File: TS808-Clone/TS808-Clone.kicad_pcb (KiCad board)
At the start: 2 copper layers, 78.7 x 147.3 mm, 44 parts, among them J1 AudioJack2, J2 Barrel_Jack, J3 AudioJack2, Q1 2N4401-AP, Q2 2N4401-AP, U1 RC4558

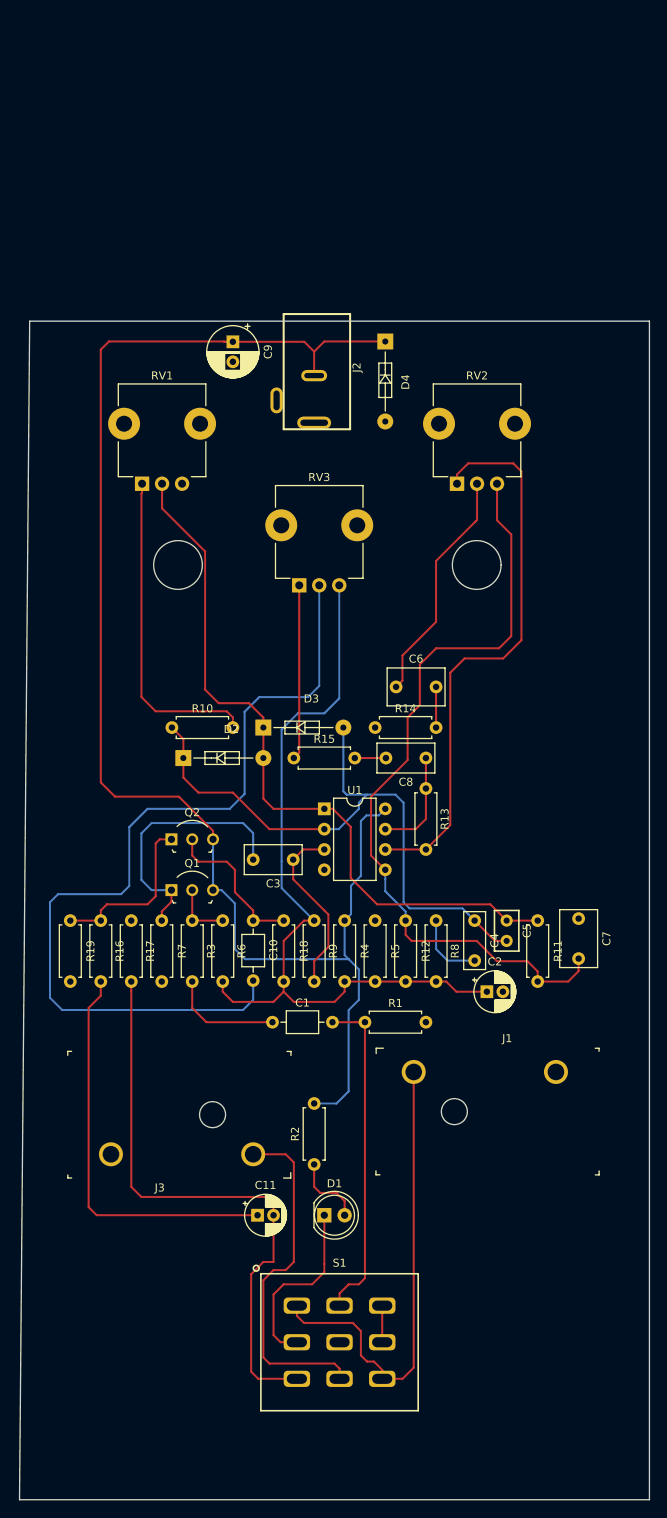
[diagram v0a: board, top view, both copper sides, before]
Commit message: Generally rearranged tracks and a couple componenets. Removed holes.
Is now cleaner. Holes+standoffs were not needed because the pots are panel mount.
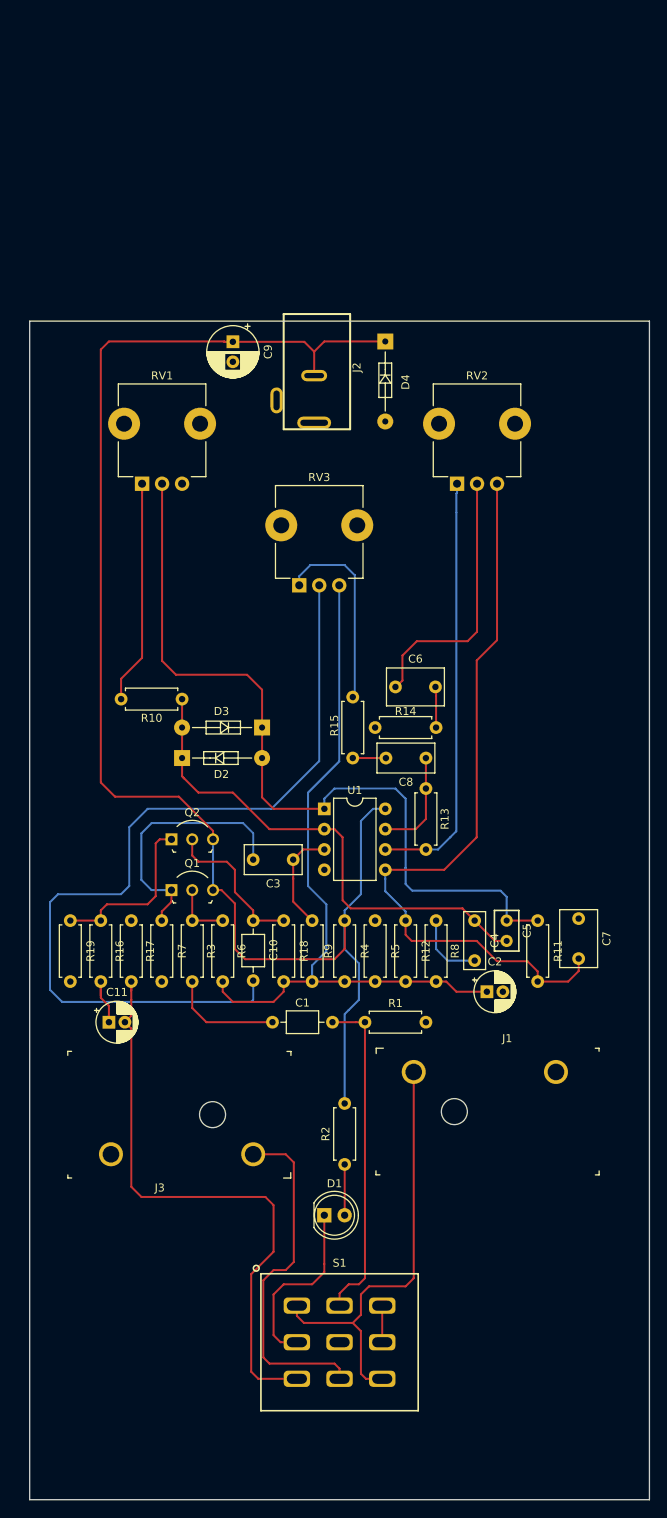
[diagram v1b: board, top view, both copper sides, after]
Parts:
- moved C11 30.5 mm to (100.1, 109.2)
- moved R15 10.6 mm to (130.6, 68.6), turned to 270 degrees
- moved R9 7.62 mm to (125.5, 104.1), turned to 90 degrees
- moved R2 3.81 mm to (129.5, 127.0)
- moved R10 3.78 mm to (109.2, 68.8), turned to 180 degrees
- moved D2 0.16 mm to (109.2, 76.2)
- moved D3 0.16 mm to (119.2, 72.4), turned to 180 degrees
- moved C6 0.08 mm to (135.9, 67.3)
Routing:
- net Net-(C11-Pad1): track 50.4 -> 7.28 mm
- net Net-(R13-Pad2): track 70.3 -> 53.3 mm
- net Net-(C4-Pad1): track 78.1 -> 63.5 mm
- net Net-(R10-Pad2): track 40.5 -> 29.2 mm
- net Net-(C5-Pad1): track 91.2 -> 101.5 mm
- net Net-(C3-Pad1): track 22.2 -> 13.1 mm
- net Net-(C2-Pad1): track 97.9 -> 90.0 mm
- net Net-(C6-Pad1): track 29.6 -> 33.3 mm
- net Net-(J1-PadT): track 59.1 -> 55.5 mm
- net Net-(D1-Pad2): track 9.12 -> 5.59 mm
- net Net-(C7-Pad2): track 97.7 -> 94.4 mm
- net Net-(R15-Pad1): track 21.9 -> 24.4 mm
- net Net-(C10-Pad1): track 108.7 -> 106.7 mm
- net Net-(C11-Pad2): track 73.2 -> 74.2 mm
- net VS: track 186.5 -> 187.1 mm
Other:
- board size 78.7 x 147.3 mm -> 77.5 x 147.3 mm
- rule trace_min: 0.1524 -> 0.2032

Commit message: Finished traces. Added fill with ground layer.
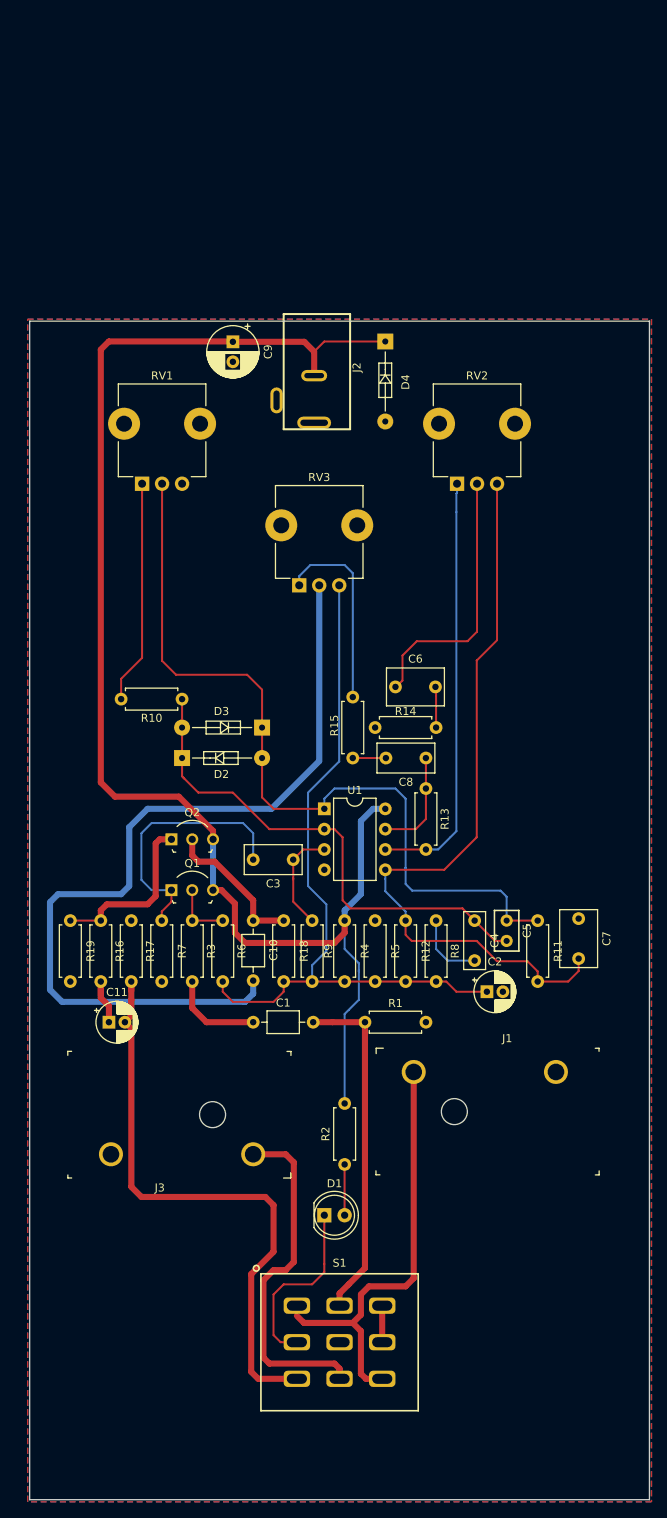
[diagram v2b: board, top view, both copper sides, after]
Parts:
- moved C1 2.41 mm to (118.1, 109.2)
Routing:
- net VS: track 187.1 -> 184.0 mm
- net Net-(C1-Pad1): track 14.1 -> 11.7 mm
- net Net-(C1-Pad2): track 41.6 -> 43.2 mm
- net Net-(C10-Pad2): track 19.2 -> 18.3 mm
- added copper zone on B.Cu, net GNDREF
- added copper zone on F.Cu, net GNDREF
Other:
- net class Default: clearance 0.2 -> 0.2032; trace_width 0.25 -> 0.762
- rule trace_clearance: 0.2 -> 0.2032

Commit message: trying a redesign of the layout
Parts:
- RV1: value 500k -> 500k LOG
- RV2: value 20k -> 20k LIN
- RV3: value 100k -> 100k LOG
- moved R5 112.5 mm to (138.6, -8.19), turned to 0 degrees
- moved R4 108.3 mm to (127.9, -4.14), turned to 0 degrees
- moved C2 108.2 mm to (161.0, -1.89)
- moved R17 67.1 mm to (114.9, 162.6), turned to 90 degrees
- moved R18 61.6 mm to (130.8, 43.2), turned to 270 degrees
- moved C10 61.4 mm to (127.0, 43.3), turned to 270 degrees
- moved R11 59.4 mm to (114.3, 59.7)
- moved C5 58.4 mm to (106.7, 58.4)
- moved C4 56.6 mm to (102.9, 59.6), turned to 90 degrees
- moved R14 49.8 mm to (163.8, 33.0), turned to 270 degrees
- moved Q2 47.6 mm to (121.2, 132.1)
- moved R8 44.1 mm to (111.8, 63.5)
- moved R16 43.6 mm to (114.9, 137.2)
- moved C11 41.9 mm to (114.3, 148.6), turned to 270 degrees
- moved C7 41.3 mm to (127.0, 69.8), turned to 0 degrees
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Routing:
- net VS: track 184.0 -> 0.00 mm
- net Net-(C10-Pad1): track 106.3 -> 0.00 mm
- net Net-(C5-Pad1): track 101.5 -> 0.00 mm
- net Net-(C7-Pad2): track 94.4 -> 0.00 mm
- net Net-(C2-Pad1): track 90.0 -> 0.00 mm
- net Net-(C11-Pad2): track 74.2 -> 0.00 mm
- net Net-(C4-Pad1): track 63.5 -> 0.00 mm
- net Net-(J1-PadT): track 55.5 -> 0.00 mm
- net Net-(R13-Pad2): track 53.3 -> 0.00 mm
- net Net-(J3-PadT): track 43.7 -> 0.00 mm
- net Net-(C1-Pad2): track 43.2 -> 0.00 mm
- net Net-(C6-Pad1): track 33.3 -> 0.00 mm
- net Net-(C3-Pad2): track 32.8 -> 0.00 mm
- net Net-(R10-Pad2): track 29.2 -> 0.00 mm
- net Net-(R15-Pad1): track 24.3 -> 0.00 mm
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
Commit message: moved jacks to final positions
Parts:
- D1: footprint LED_THT:LED_D5.0mm -> LED_SMD:LED_1206_3216Metric_Pad1.42x1.75mm_HandSolder
- J1, J2, J3: moved to B.Cu
- RV1, RV2, RV3: footprint Potentiometer_THT:Potentiometer_TT_P0915N -> TS808-Clone:Potentiometer_BournesProAudio_THT_vert
- S1: footprint TS808-Clone:Switch_3P3T_Footswitch_PC_THT -> TS808-Clone:Switch_3PDT_ESwitch_300_P1J1_VS2
- moved J1 73.2 mm to (147.1, 32.8), turned to 90 degrees
- moved J3 72.9 mm to (107.7, 32.8), turned to 90 degrees
- moved C10 39.5 mm to (129.5, 82.7)
- moved C3 39.5 mm to (118.1, 102.9)
- moved C4 39.5 mm to (105.4, 99.0)
- moved C5 39.5 mm to (109.2, 97.8)
- moved C7 39.5 mm to (129.5, 109.2)
- moved C8 39.5 mm to (143.5, 94.1)
- moved D2 39.5 mm to (120.7, 99.1)
- moved D3 39.5 mm to (124.2, 88.9)
- moved R10 39.5 mm to (113.0, 99.1)
- moved R11 39.5 mm to (116.8, 99.1)
- moved R13 39.5 mm to (139.7, 94.0)
- moved R15 39.5 mm to (147.3, 94.0)
- moved R7 39.5 mm to (110.5, 102.9)
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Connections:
- U1 pad 4: GNDREF -> (no net)
- U1 pad 8: VS -> (no net)
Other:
- board size 77.5 x 147.3 mm -> 77.5 x 133 mm

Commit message: Tentative final design
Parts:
- added REF**: M3_MountingHole, TS808-Clone:M3_MountingHole, F.Cu at (106.2, 137.7)
- added REF**: M3_MountingHole, TS808-Clone:M3_MountingHole, F.Cu at (146.1, 137.7)
- added REF**: M3_MountingHole, TS808-Clone:M3_MountingHole, F.Cu at (113.5, 55.1)
- added REF**: M3_MountingHole, TS808-Clone:M3_MountingHole, F.Cu at (138.7, 55.1)
- C11, C2, C9: moved to B.Cu
- moved C2 78.4 mm to (95.8, 41.7), turned to 90 degrees
- moved Q2 64.1 mm to (94.7, 73.7), turned to 90 degrees
- moved R5 52.5 mm to (122.2, 41.7)
- moved R2 50.8 mm to (129.3, 81.8), turned to 180 degrees
- moved D4 50.0 mm to (135.4, 36.6), turned to 90 degrees
- moved C9 45.2 mm to (95.6, 33.9), turned to 90 degrees
- moved D1 44.6 mm to (126.4, 87.6)
- moved R4 42.6 mm to (122.2, 38.1)
- moved R17 36.8 mm to (117.2, 125.9), turned to 180 degrees
- moved R15 35.9 mm to (130.3, 62.4)
- moved R14 35.8 mm to (135.4, 39.5)
- moved C11 31.7 mm to (101.5, 119.6)
- moved R16 31.4 mm to (101.5, 108.8)
- moved R19 31.1 mm to (101.5, 98.9)
- moved R1 26.3 mm to (109.6, 122.6), turned to 0 degrees
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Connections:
- U1 pad 4: (no net) -> GNDREF
- U1 pad 8: (no net) -> VS
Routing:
- net VS: track 0.00 -> 181.6 mm
- net Net-(J1-PadT): track 0.00 -> 140.5 mm
- net Net-(J3-PadT): track 0.00 -> 137.9 mm, vias 0 -> 1
- net Net-(C2-Pad1): track 0.00 -> 123.2 mm, vias 0 -> 1
- net Net-(C7-Pad2): track 0.00 -> 118.8 mm
- net Net-(C5-Pad1): track 0.00 -> 73.3 mm
- net Net-(R13-Pad2): track 0.00 -> 72.1 mm
- net Net-(D1-Pad1): track 0.00 -> 45.7 mm
- net Net-(Q2-Pad1): track 0.00 -> 40.7 mm
- net Net-(R10-Pad2): track 0.00 -> 38.4 mm
- net Net-(C1-Pad2): track 0.00 -> 38.1 mm
- net Net-(C10-Pad2): track 0.00 -> 31.5 mm, vias 0 -> 1
- net Net-(C3-Pad2): track 0.00 -> 29.7 mm
- net Net-(C11-Pad2): track 0.00 -> 25.9 mm
- net Net-(C4-Pad1): track 0.00 -> 25.3 mm
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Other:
- board size 77.5 x 133 mm -> 72 x 133 mm
